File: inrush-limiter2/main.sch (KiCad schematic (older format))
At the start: 32 parts

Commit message: fix up annotation
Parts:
- gave numbers to parts that had none: 19
- renumbered CP to CP1, D to D7, R to R1, R to R10, R to R11, R to R12, R to R2, R to R3, R to R5, R to R6, R to R9, RVAR to RVAR1
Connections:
- wire segments 118 -> 83

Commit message: update
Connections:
- wire segments 83 -> 89
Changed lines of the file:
@@
 	5650 4650 5400 4650
 Connection ~ 3750 5900
-Connection ~ 3750 4350
-Wire Wire Line
-	3750 4350 3750 4700
 Connection ~ 3100 4900
 Connection ~ 1600 5100
@@
 Wire Wire Line
 	2250 5900 2250 5800
-Connection ~ 2250 4350
-Wire Wire Line
-	2250 4350 2250 4550
 Connection ~ 5200 3000
 Wire Wire Line
@@
 Wire Wire Line
 	3400 1050 3500 1050
+Wire Wire Line
+	3750 4700 3750 4350
+Connection ~ 3750 4350
+Wire Wire Line
+	5650 4950 5550 4950
+Wire Wire Line
+	5550 4950 5550 5200
+Wire Wire Line
+	5550 5200 6600 5200
+Wire Wire Line
+	6600 5200 6600 4850
+Wire Wire Line
+	6600 4850 6450 4850
+Wire Wire Line
+	6450 5050 6600 5050
+Connection ~ 6600 5050
+Wire Wire Line
+	2250 4500 2250 4350
+Connection ~ 2250 4350
 $EndSCHEMATC

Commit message: adjust component positions
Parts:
- CP1: footprint (none) -> Capacitors_ThroughHole:C_Rect_L7_W3.5_P5
- D6: footprint (none) -> LEDs:LED-5MM
- D7: footprint (none) -> Diodes_ThroughHole:Diode_DO-35_SOD27_Horizontal_RM10
- MOV1, U2: footprint (none) -> Resistors_ThroughHole:Resistor_Horizontal_RM10mm
- Q1, Q2: footprint (none) -> TO_SOT_Packages_THT:TO-92_Inline_Wide
- R10, R11, R12, R2, R3, R4, R5, R6, R9, RVAR1: footprint (none) -> Resistors_ThroughHole:Resistor_Horizontal_RM7mm
- T1: footprint (none) -> Transformers_CHK:Trafo_CHK-EI30-2VA_1xSec
- U1: footprint (none) -> Housings_DIP:DIP-8_W7.62mm
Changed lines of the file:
@@
 F 0 "Q2" H 6000 2575 50  0000 L CNN
 F 1 "PN2222A" H 6000 2500 50  0000 L CNN
-F 2 "" H 6000 2425 50  0000 L CIN
+F 2 "TO_SOT_Packages_THT:TO-92_Inline_Wide" H 6000 2425 50  0001 L CIN
 F 3 "" H 5800 2500 50  0000 L CNN
 	1    5800 2500
@@
 F 0 "D7" H 5200 3400 50  0000 C CNN
 F 1 "5.6V" H 5200 3200 50  0000 C CNN
-F 2 "" H 5200 3300 50  0000 C CNN
+F 2 "Diodes_ThroughHole:Diode_DO-35_SOD27_Horizontal_RM10" H 5200 3300 50  0001 C CNN
 F 3 "" H 5200 3300 50  0000 C CNN
 	1    5200 3300
@@
 F 0 "R11" V 5280 2750 50  0000 C CNN
 F 1 "2k" V 5200 2750 50  0000 C CNN
-F 2 "" V 5130 2750 50  0000 C CNN
+F 2 "Resistors_ThroughHole:Resistor_Horizontal_RM7mm" V 5130 2750 50  0001 C CNN
 F 3 "" H 5200 2750 50  0000 C CNN
 	1    5200 2750
@@
 F 0 "R2" V 1680 4750 50  0000 C CNN
 F 1 "100k" V 1600 4750 50  0000 C CNN
-F 2 "" V 1530 4750 50  0000 C CNN
+F 2 "Resistors_ThroughHole:Resistor_Horizontal_RM7mm" V 1530 4750 50  0001 C CNN
 F 3 "" H 1600 4750 50  0000 C CNN
 	1    1600 4750
@@
 F 0 "R3" V 1680 5450 50  0000 C CNN
 F 1 "100k" V 1600 5450 50  0000 C CNN
-F 2 "" V 1530 5450 50  0000 C CNN
+F 2 "Resistors_ThroughHole:Resistor_Horizontal_RM7mm" V 1530 5450 50  0001 C CNN
 F 3 "" H 1600 5450 50  0000 C CNN
 	1    1600 5450
@@
 F 0 "R4" V 2330 4650 50  0000 C CNN
 F 1 "100k" V 2250 4650 50  0000 C CNN
-F 2 "" V 2180 4650 50  0000 C CNN
+F 2 "Resistors_ThroughHole:Resistor_Horizontal_RM7mm" V 2180 4650 50  0001 C CNN
 F 3 "" H 2250 4650 50  0000 C CNN
 	1    2250 4650
@@
 F 0 "R5" V 2330 5300 50  0000 C CNN
 F 1 "10k" V 2250 5300 50  0000 C CNN
-F 2 "" V 2180 5300 50  0000 C CNN
+F 2 "Resistors_ThroughHole:Resistor_Horizontal_RM7mm" V 2180 5300 50  0001 C CNN
 F 3 "" H 2250 5300 50  0000 C CNN
 	1    2250 5300
@@
 F 0 "R6" V 2330 5650 50  0000 C CNN
 F 1 "100k" V 2250 5650 50  0000 C CNN
-F 2 "" V 2180 5650 50  0000 C CNN
+F 2 "Resistors_ThroughHole:Resistor_Horizontal_RM7mm" V 2180 5650 50  0001 C CNN
 F 3 "" H 2250 5650 50  0000 C CNN
 	1    2250 5650
@@
 F 0 "RVAR1" V 2730 4850 50  0000 C CNN
 F 1 "1M" V 2570 4960 50  0000 C CNN
-F 2 "" H 2650 4900 50  0000 C CNN
+F 2 "Resistors_ThroughHole:Resistor_Horizontal_RM7mm" H 2650 4900 50  0001 C CNN
 F 3 "" H 2650 4900 50  0000 C CNN
 	1    2650 4900
@@
 F 0 "CP1" H 3125 5550 50  0000 L CNN
 F 1 "470nF" H 3125 5350 50  0000 L CNN
-F 2 "" H 3138 5300 50  0000 C CNN
+F 2 "Capacitors_ThroughHole:C_Rect_L7_W3.5_P5" H 3138 5300 50  0001 C CNN
 F 3 "" H 3100 5450 50  0000 C CNN
 	1    3100 5450
@@
 F 0 "U1" H 4000 5150 50  0000 C CNN
 F 1 "LM393" H 4100 4850 50  0000 C CNN
-F 2 "" H 3850 5000 50  0000 C CNN
+F 2 "Housings_DIP:DIP-8_W7.62mm" H 3850 5000 50  0001 C CNN
 F 3 "" H 3850 5000 50  0000 C CNN
 	1    3850 5000
@@
 F 0 "R9" V 4630 4650 50  0000 C CNN
 F 1 "2k" V 4550 4650 50  0000 C CNN
-F 2 "" V 4480 4650 50  0000 C CNN
+F 2 "Resistors_ThroughHole:Resistor_Horizontal_RM7mm" V 4480 4650 50  0001 C CNN
 F 3 "" H 4550 4650 50  0000 C CNN
 	1    4550 4650
@@
 F 0 "Q1" H 4700 5875 40  0000 C CNN
 F 1 "2N3904" H 4675 5800 40  0000 L CNN
-F 2 "" H 4550 5800 60  0000 C CNN
+F 2 "TO_SOT_Packages_THT:TO-92_Inline_Wide" H 4550 5800 60  0001 C CNN
 F 3 "" H 4550 5800 60  0000 C CNN
 	1    4550 5800
@@
 F 0 "D6" H 4950 5500 50  0000 C CNN
 F 1 "LED" H 4950 5300 50  0000 C CNN
-F 2 "" H 4950 5400 50  0000 C CNN
+F 2 "LEDs:LED-5MM" H 4950 5400 50  0001 C CNN
 F 3 "" H 4950 5400 50  0000 C CNN
 	1    4950 5400
@@
 F 0 "R10" V 5030 4800 50  0000 C CNN
 F 1 "140" V 4950 4800 50  0000 C CNN
-F 2 "" V 4880 4800 50  0000 C CNN
+F 2 "Resistors_ThroughHole:Resistor_Horizontal_RM7mm" V 4880 4800 50  0001 C CNN
 F 3 "" H 4950 4800 50  0000 C CNN
 	1    4950 4800
@@
 F 0 "T1" H 2200 2450 50  0000 C CNN
 F 1 "TRANSFO" H 2200 1900 50  0000 C CNN
-F 2 "" H 2200 2200 50  0000 C CNN
+F 2 "Transformers_CHK:Trafo_CHK-EI30-2VA_1xSec" H 2200 2200 50  0001 C CNN
 F 3 "" H 2200 2200 50  0000 C CNN
 	1    2200 2200
@@
 F 0 "U2" V 6880 4750 50  0000 C CNN
 F 1 "50 ohm NTC" V 6800 4750 50  0000 C CNN
-F 2 "" V 6730 4750 50  0000 C CNN
+F 2 "Resistors_ThroughHole:Resistor_Horizontal_RM10mm" V 6730 4750 50  0001 C CNN
 F 3 "" H 6800 4750 50  0000 C CNN
 	1    6800 4750
@@
 F 0 "U1" H 4000 6850 50  0000 C CNN
 F 1 "LM393" H 4100 6550 50  0000 C CNN
-F 2 "" H 3850 6700 50  0000 C CNN
+F 2 "Housings_DIP:DIP-8_W7.62mm" H 3850 6700 50  0001 C CNN
 F 3 "" H 3850 6700 50  0000 C CNN
 	2    3850 6700
@@
 F 0 "MOV1" V 2730 1050 50  0000 C CNN
 F 1 "MOV" V 2650 1050 50  0000 C CNN
-F 2 "" V 2580 1050 50  0000 C CNN
+F 2 "Resistors_ThroughHole:Resistor_Horizontal_RM10mm" V 2580 1050 50  0001 C CNN
 F 3 "" H 2650 1050 50  0000 C CNN
 	1    2650 1050
@@
 F 0 "R12" V 6380 2400 50  0000 C CNN
 F 1 "0" V 6300 2400 50  0000 C CNN
-F 2 "" V 6230 2400 50  0000 C CNN
+F 2 "Resistors_ThroughHole:Resistor_Horizontal_RM7mm" V 6230 2400 50  0001 C CNN
 F 3 "" H 6300 2400 50  0000 C CNN
 	1    6300 2400

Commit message: update
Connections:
- wire segments 89 -> 87
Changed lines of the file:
@@
-	1    0    0    -1
-$EndComp
-$Comp
-L +5V #PWR01
-U 1 1 57C1B997
-P 1150 4050
-F 0 "#PWR01" H 1150 3900 50  0001 C CNN
-F 1 "+5V" H 1150 4190 50  0000 C CNN
-F 2 "" H 1150 4050 50  0000 C CNN
-F 3 "" H 1150 4050 50  0000 C CNN
-	1    1150 4050
-	1    0    0    -1
-$EndComp
-$Comp
-L GND #PWR02
-U 1 1 57C1BA06
-P 1150 6200
-F 0 "#PWR02" H 1150 5950 50  0001 C CNN
-F 1 "GND" H 1150 6050 50  0000 C CNN
-F 2 "" H 1150 6200 50  0000 C CNN
-F 3 "" H 1150 6200 50  0000 C CNN
-	1    1150 6200
 	1    0    0    -1
 $EndComp
@@
 	1    0    0    -1
 $EndComp
-$Comp
-L +5V #PWR03
-U 1 1 57CC9197
-P 6550 2150
-F 0 "#PWR03" H 6550 2000 50  0001 C CNN
-F 1 "+5V" H 6550 2290 50  0000 C CNN
-F 2 "" H 6550 2150 50  0000 C CNN
-F 3 "" H 6550 2150 50  0000 C CNN
-	1    6550 2150
-	1    0    0    -1
-$EndComp
-$Comp
-L GND #PWR04
-U 1 1 57CC91E5
-P 6550 3850
-F 0 "#PWR04" H 6550 3600 50  0001 C CNN
-F 1 "GND" H 6550 3700 50  0000 C CNN
-F 2 "" H 6550 3850 50  0000 C CNN
-F 3 "" H 6550 3850 50  0000 C CNN
-	1    6550 3850
-	1    0    0    -1
-$EndComp
 Text GLabel 7200 4550 2    60   Input ~ 0
 AC-live-f
@@
 Wire Wire Line
 	2650 900  2650 750
-Connection ~ 3750 7100
-Wire Wire Line
-	3750 7000 3750 7450
 Connection ~ 3250 6800
 Wire Wire Line
-	3250 7100 3750 7100
-Wire Wire Line
 	3250 6800 3550 6800
 Wire Wire Line
-	3250 6600 3250 7100
+	3250 6600 3250 7250
 Wire Wire Line
 	3550 6600 3250 6600
@@
 	1150 5600 1150 6200
 Wire Wire Line
-	1150 4000 1150 4700
+	1150 4050 1150 4700
 Wire Wire Line
 	5400 5550 5600 5550
@@
 Wire Wire Line
 	3100 2400 3100 3650
-$Comp
-L GND #PWR05
-U 1 1 57CE7D0C
-P 3750 7500
-F 0 "#PWR05" H 3750 7250 50  0001 C CNN
-F 1 "GND" H 3750 7350 50  0000 C CNN
-F 2 "" H 3750 7500 50  0000 C CNN
-F 3 "" H 3750 7500 50  0000 C CNN
-	1    3750 7500
-	1    0    0    -1
-$EndComp
 $Comp
 L R R12
@@
 	6450 2400 6550 2400
 Wire Wire Line
-	3750 6200 3750 6400
-$Comp
-L +5V #PWR06
-U 1 1 57CE86AC
-P 3750 6200
-F 0 "#PWR06" H 3750 6050 50  0001 C CNN
-F 1 "+5V" H 3750 6340 50  0000 C CNN
-F 2 "" H 3750 6200 50  0000 C CNN
-F 3 "" H 3750 6200 50  0000 C CNN
-	1    3750 6200
-	1    0    0    -1
-$EndComp
-Wire Wire Line
 	4350 3100 4350 3650
 Wire Wire Line
@@
 	2250 4500 2250 4350
 Connection ~ 2250 4350
+Text GLabel 6550 2150 2    60   Input ~ 0
++5V
+Text GLabel 6550 3850 2    60   Input ~ 0
+GND
+Text GLabel 1100 4050 0    60   Input ~ 0
++5V
+Wire Wire Line
+	1100 4050 1150 4050
+Text GLabel 1150 6200 0    60   Input ~ 0
+GND
+Text GLabel 3250 7250 0    60   Input ~ 0
+GND
 $EndSCHEMATC

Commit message: use pot
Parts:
- removed RVAR1: 1M, Resistors_ThroughHole:Resistor_Horizontal_RM7mm, symbol RVAR
- added RV1: POT, symbol POT
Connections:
- net at R4.2, R5.1: now also RV1.3
- net at CP1.1, U1.3 (+): now also RV1.2
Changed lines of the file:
@@
-$EndComp
-$Comp
-L RVAR RVAR1
-U 1 1 57CC0108
-P 2650 4900
-F 0 "RVAR1" V 2730 4850 50  0000 C CNN
-F 1 "1M" V 2570 4960 50  0000 C CNN
-F 2 "Resistors_ThroughHole:Resistor_Horizontal_RM7mm" H 2650 4900 50  0001 C CNN
-F 3 "" H 2650 4900 50  0000 C CNN
-	1    2650 4900
-	0    1    1    0
 $EndComp
 $Comp
@@
 Connection ~ 2250 4900
 Wire Wire Line
-	2400 4900 2250 4900
+	2250 4900 2550 4900
 Wire Wire Line
 	2250 4800 2250 5150
@@
 	5550 4950 5550 5200
 Wire Wire Line
-	5550 5200 6600 5200
-Wire Wire Line
-	6600 5200 6600 4850
+	6600 5200 5550 5200
+Wire Wire Line
+	6600 4850 6600 5200
 Wire Wire Line
 	6600 4850 6450 4850
@@
 Text GLabel 3250 7250 0    60   Input ~ 0
 GND
+$Comp
+L POT RV1
+U 1 1 57CFC846
+P 2900 4750
+F 0 "RV1" H 2900 4670 50  0000 C CNN
+F 1 "POT" H 2900 4750 50  0000 C CNN
+F 2 "" H 2900 4750 50  0000 C CNN
+F 3 "" H 2900 4750 50  0000 C CNN
+	1    2900 4750
+	-1   0    0    1
+$EndComp
+Wire Wire Line
+	2750 4750 2550 4750
+Wire Wire Line
+	2550 4750 2550 4900
 $EndSCHEMATC

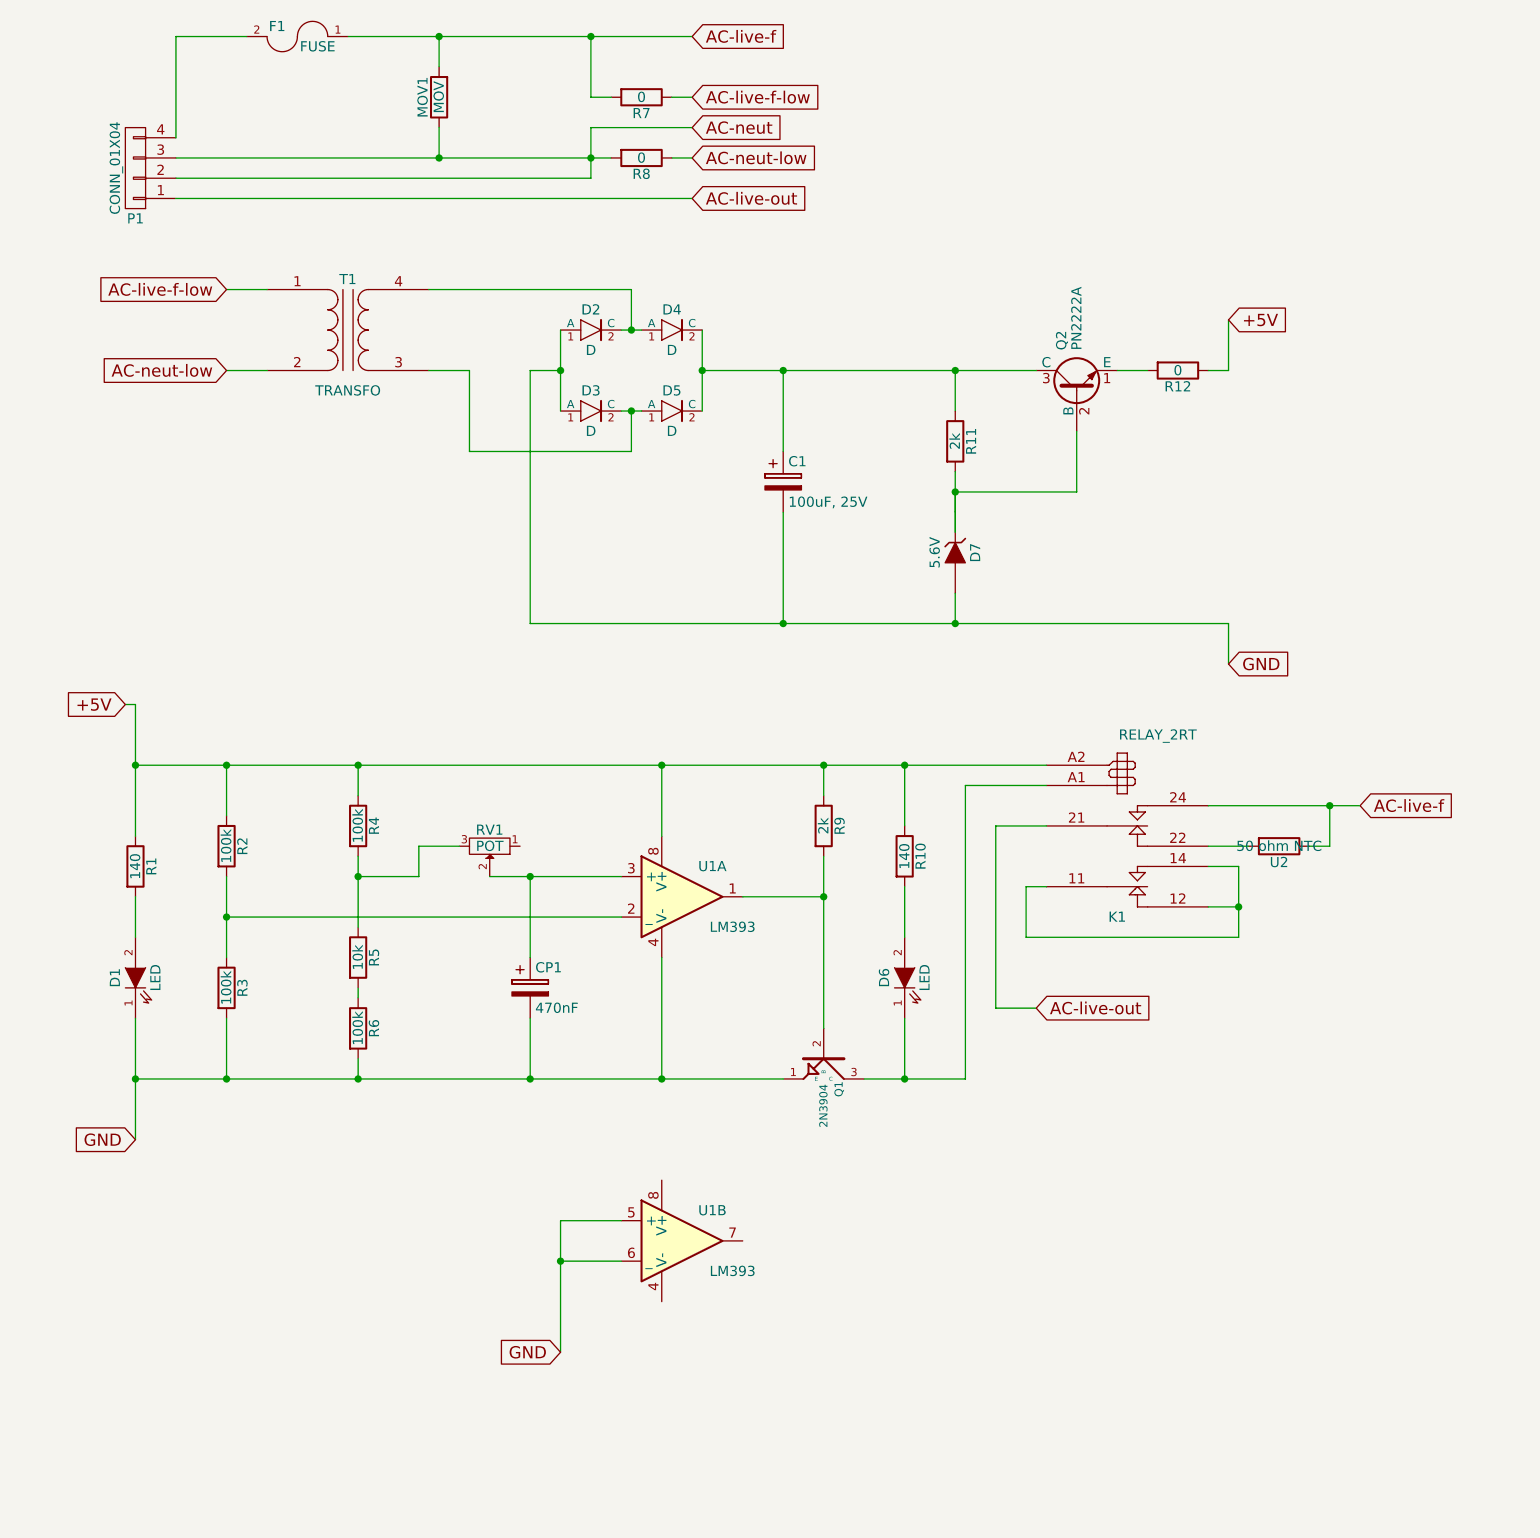
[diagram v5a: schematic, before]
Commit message: add custom footprint for terminal block
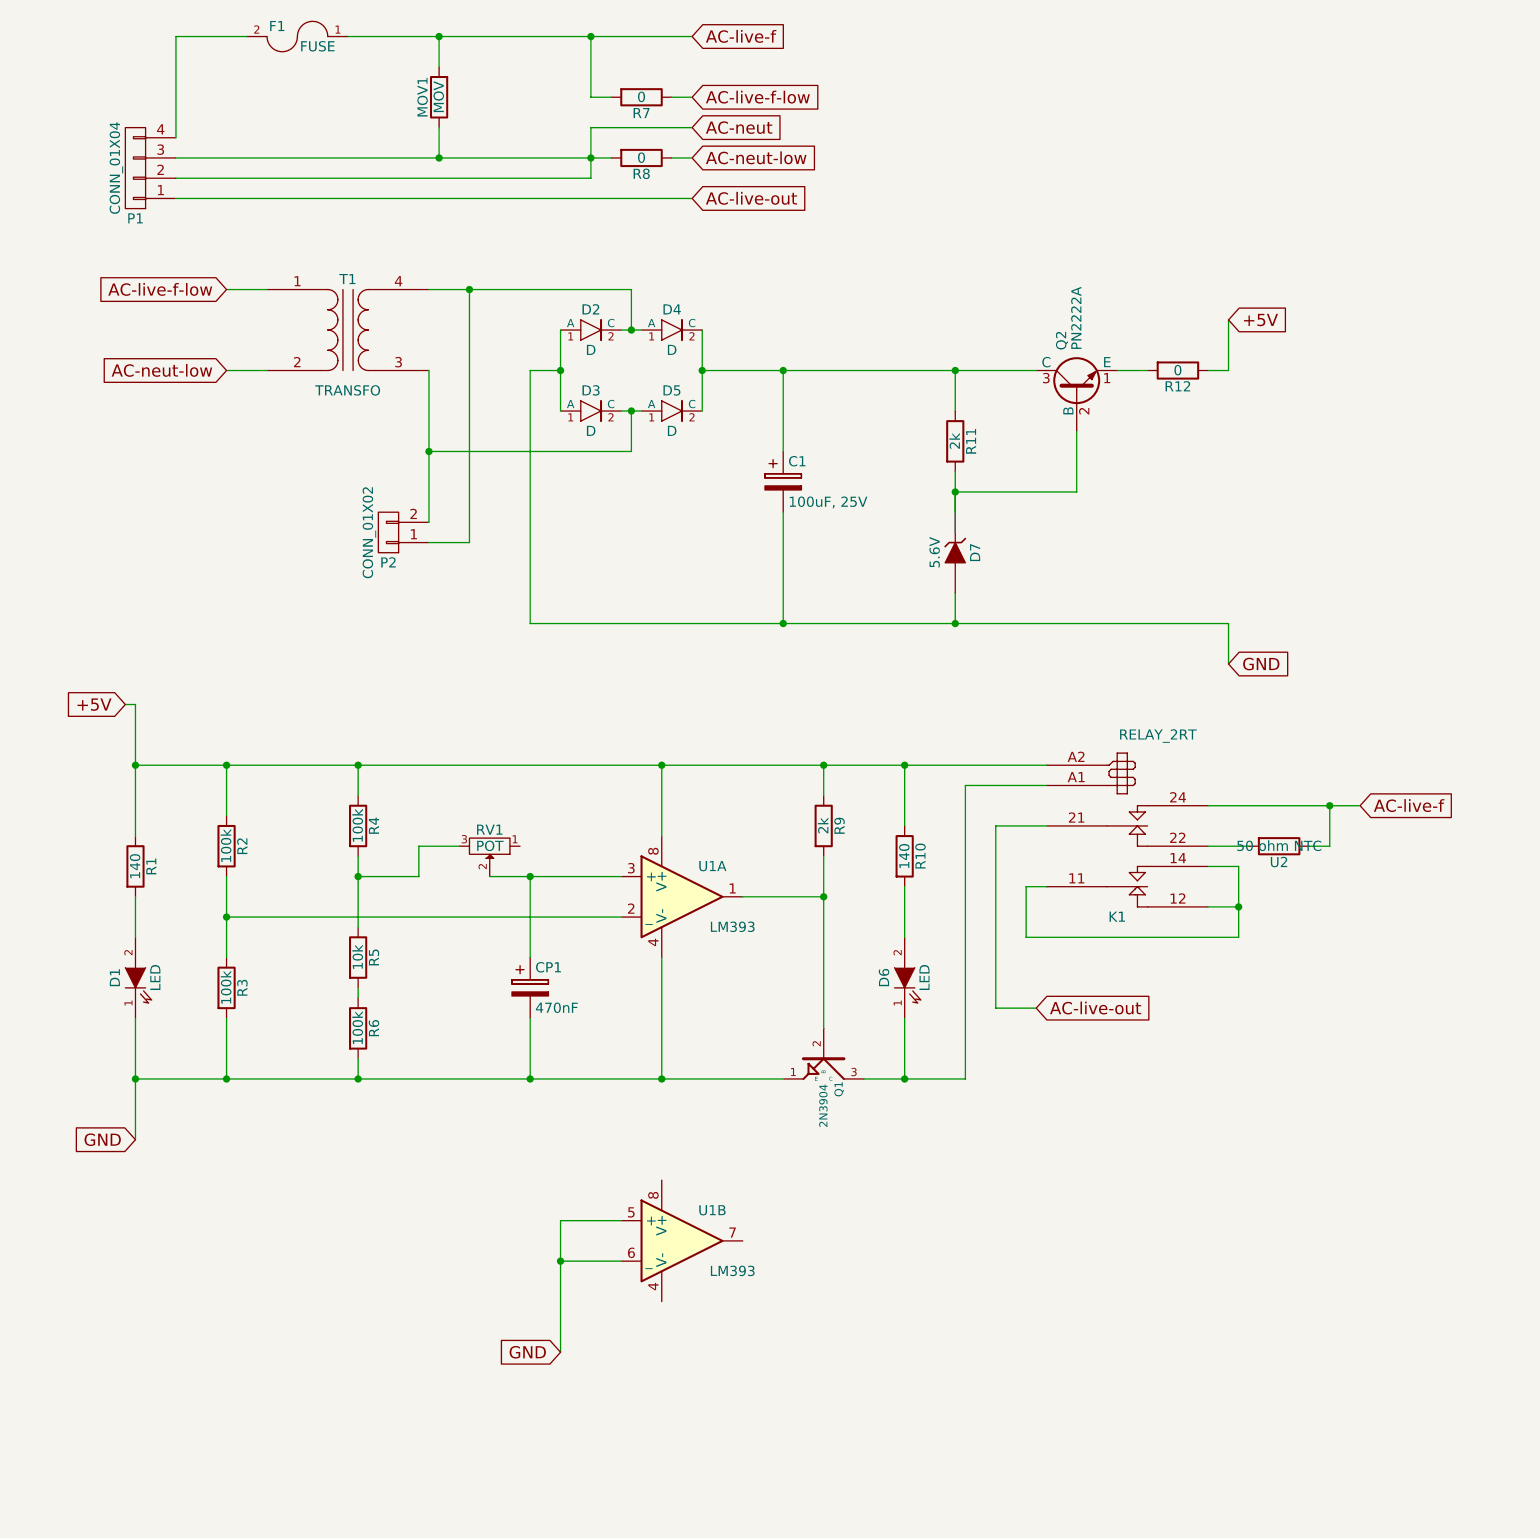
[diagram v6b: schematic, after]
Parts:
- added P2: CONN_01X02, symbol CONN_01X02
- P1: footprint Connect:AK300-4 -> Terminal_Blocks:TerminalBlock_WAGO-804_RM7.5mm_3pol
- RV1: footprint (none) -> Potentiometers:Potentiometer_Bourns_3296W_3-8Zoll_Inline_ScrewUp
- T1: footprint Transformers_CHK:Trafo_CHK-EI30-2VA_1xSec -> Transformers_CHK:Trafo_CHK-EI30-2VA_Neutral
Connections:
- net at D2.2 (C), D4.1 (A), T1.4 (SB): now also P2.1 (P1)
- net at D3.2 (C), D5.1 (A), T1.3 (SA): now also P2.2 (P2)
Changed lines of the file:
@@
 F 0 "P1" H 1150 1650 50  0000 C CNN
 F 1 "CONN_01X04" V 1250 1400 50  0000 C CNN
-F 2 "Connect:AK300-4" H 1150 1400 50  0001 C CNN
+F 2 "Terminal_Blocks:TerminalBlock_WAGO-804_RM7.5mm_3pol" H 1150 1400 50  0001 C CNN
 F 3 "" H 1150 1400 50  0000 C CNN
 	1    1150 1400
@@
 F 0 "T1" H 2200 2450 50  0000 C CNN
 F 1 "TRANSFO" H 2200 1900 50  0000 C CNN
-F 2 "Transformers_CHK:Trafo_CHK-EI30-2VA_1xSec" H 2200 2200 50  0001 C CNN
+F 2 "Transformers_CHK:Trafo_CHK-EI30-2VA_Neutral" H 2200 2200 50  0001 C CNN
 F 3 "" H 2200 2200 50  0000 C CNN
 	1    2200 2200
@@
 	1600 2000 1800 2000
 Wire Wire Line
-	2800 2400 2800 2800
-Wire Wire Line
-	2600 2400 2800 2400
-Wire Wire Line
 	5250 5900 5250 4450
 Wire Wire Line
@@
 	1150 4350 5650 4350
 Wire Wire Line
-	2800 2800 3600 2800
+	2600 2800 3600 2800
 Connection ~ 4350 2400
 Wire Wire Line
@@
 	5550 4950 5550 5200
 Wire Wire Line
-	6600 5200 5550 5200
-Wire Wire Line
-	6600 4850 6600 5200
+	5550 5200 6600 5200
+Wire Wire Line
+	6600 5200 6600 4850
 Wire Wire Line
 	6600 4850 6450 4850
@@
 F 0 "RV1" H 2900 4670 50  0000 C CNN
 F 1 "POT" H 2900 4750 50  0000 C CNN
-F 2 "" H 2900 4750 50  0000 C CNN
+F 2 "Potentiometers:Potentiometer_Bourns_3296W_3-8Zoll_Inline_ScrewUp" H 2900 4750 50  0001 C CNN
 F 3 "" H 2900 4750 50  0000 C CNN
 	1    2900 4750
@@
 Wire Wire Line
 	2550 4750 2550 4900
+$Comp
+L CONN_01X02 P2
+U 1 1 57CFF614
+P 2400 3200
+F 0 "P2" H 2400 3350 50  0000 C CNN
+F 1 "CONN_01X02" V 2500 3200 50  0000 C CNN
+F 2 "" H 2400 3200 50  0000 C CNN
+F 3 "" H 2400 3200 50  0000 C CNN
+	1    2400 3200
+	-1   0    0    1
+$EndComp
+Wire Wire Line
+	2600 2400 2600 3150
+Connection ~ 2600 2800
+Wire Wire Line
+	2600 3250 2800 3250
+Wire Wire Line
+	2800 3250 2800 2000
+Connection ~ 2800 2000
 $EndSCHEMATC
